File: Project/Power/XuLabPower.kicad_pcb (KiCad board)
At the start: 2 copper layers, 100 x 119 mm, 178 parts, among them J1 Servo, J10 Battery, J11 Battery, J12 Battery, J13 I2C, J14 SWD, J15 SPI1, J16 5V_2A, J17 5V_6A, J2 Servo, J3 Servo, J4 Servo, J5 Servo, J6 Servo, J7 Servo, J8 Servo, J9 Battery, Q1 SQJ138ELP, Q2 SQJ138ELP, Q3 SQJ138ELP, Q4 SQJ138ELP, Q5 SQJ138ELP, Q6 SQJ138ELP, SW1 SW_Push, U1 LM74502, U10 INA199B3DCKR, U11 TL331, U12 INA199B3DCKR, U13 TL331, U14 STM32L422KBTx, U15 TPS560200, U16 MIC5219-3.3YM5, U17 TPS562200, U18 TPS54627, U19 INA226, U2 NCV68061, U20 INA226, U21 INA226, U22 INA226, U23 INA226, U24 INA226, U25 INA226, U26 INA226, U3 NCV68061, U4 INA199B3DCKR, U5 TL331, U6 INA199B3DCKR, U7 TL331, U8 NCV68061, U9 NCV68061

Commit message: Add initial layout
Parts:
- C2: value 4700uF -> 2200uF; footprint Capacitor_THT:CP_Radial_D12.5mm_P5.00mm -> Capacitor_THT:CP_Radial_D18.0mm_P7.50mm
- J1, J2, J3, J4, J5, J6, J7, J8: footprint Connector_JST:JST_VH_S2P-VH_1x02_P3.96mm_Horizontal -> Connector_JST:JST_VH_B2P-VH_1x02_P3.96mm_Vertical
- J10, J11, J12, J9: footprint Connector_AMASS:AMASS_XT60PW-M_1x02_P7.20mm_Horizontal -> Connector_AMASS:AMASS_XT60-M_1x02_P7.20mm_Vertical
- moved H1 94.0 mm to (123.0, 105.0)
- moved H2 94.0 mm to (172.0, 105.0)
- moved H3 94.0 mm to (123.0, 47.0)
- moved H4 94.0 mm to (172.0, 47.0)
- moved C16 34.1 mm to (130.0, 48.0)
- moved SW1 34.1 mm to (135.0, 48.0)
- moved R39 33.0 mm to (143.0, 157.0), turned to 180 degrees
- moved R40 33.0 mm to (153.0, 123.0), turned to 0 degrees
- moved D1 31.3 mm to (120.0, 119.0), turned to 180 degrees
- moved D3 31.3 mm to (176.0, 161.0), turned to 0 degrees
- moved C10 30.5 mm to (164.0, 161.0), turned to 0 degrees
- moved C6 30.5 mm to (132.0, 119.0), turned to 180 degrees
- moved R12 30.0 mm to (124.0, 119.0), turned to 180 degrees
- moved R22 30.0 mm to (172.0, 161.0), turned to 0 degrees
- moved C13 28.0 mm to (152.0, 51.0)
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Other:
- board size 100 x 119 mm -> 74 x 148 mm

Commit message: Set stackup to six layers
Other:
- copper layers 2 -> 6
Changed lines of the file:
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@@
 	(layers
 		(0 "F.Cu" signal)
+		(4 "In1.Cu" power)
+		(6 "In2.Cu" power)
+		(8 "In3.Cu" power)
+		(10 "In4.Cu" power)
 		(2 "B.Cu" signal)
 		(9 "F.Adhes" user "F.Adhesive")
@@
 	)
 	(setup
+		(stackup
+			(layer "F.SilkS"
+				(type "Top Silk Screen")
+			)
+			(layer "F.Paste"
+				(type "Top Solder Paste")
+			)
+			(layer "F.Mask"
+				(type "Top Solder Mask")
+				(thickness 0.01)
+			)
+			(layer "F.Cu"
+				(type "copper")
+				(thickness 0.035)
+			)
+			(layer "dielectric 1"
+				(type "prepreg")
+				(thickness 0.1)
+				(material "FR4")
+				(epsilon_r 4.5)
+				(loss_tangent 0.02)
+			)
+			(layer "In1.Cu"
+				(type "copper")
+				(thickness 0.035)
+			)
+			(layer "dielectric 2"
+				(type "core")
+				(thickness 0.535)
+				(material "FR4")
+				(epsilon_r 4.5)
+				(loss_tangent 0.02)
+			)
+			(layer "In2.Cu"
+				(type "copper")
+				(thickness 0.035)
+			)
+			(layer "dielectric 3"
+				(type "prepreg")
+				(thickness 0.1)
+				(material "FR4")
+				(epsilon_r 4.5)
+				(loss_tangent 0.02)
+			)
+			(layer "In3.Cu"
+				(type "copper")
+				(thickness 0.035)
+			)
+			(layer "dielectric 4"
+				(type "core")
+				(thickness 0.535)
+				(material "FR4")
+				(epsilon_r 4.5)
+				(loss_tangent 0.02)
+			)
+			(layer "In4.Cu"
+				(type "copper")
+				(thickness 0.035)
+			)
+			(layer "dielectric 5"
+				(type "prepreg")
+				(thickness 0.1)
+				(material "FR4")
+				(epsilon_r 4.5)
+				(loss_tangent 0.02)
+			)
+			(layer "B.Cu"
+				(type "copper")
+				(thickness 0.035)
+			)
+			(layer "B.Mask"
+				(type "Bottom Solder Mask")
+				(thickness 0.01)
+			)
+			(layer "B.Paste"
+				(type "Bottom Solder Paste")
+			)
+			(layer "B.SilkS"
+				(type "Bottom Silk Screen")
+			)
+			(copper_finish "None")
+			(dielectric_constraints no)
+		)
 		(pad_to_mask_clearance 0)
 		(allow_soldermask_bridges_in_footprints no)

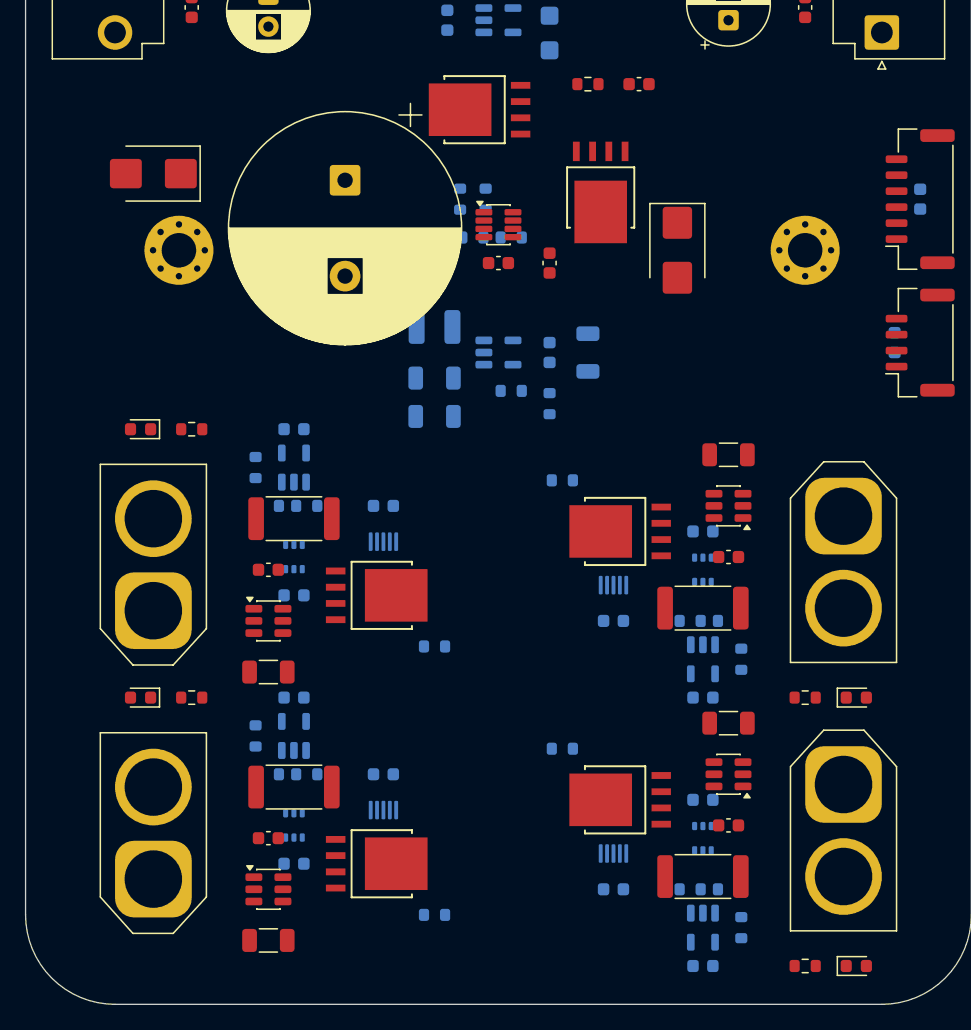
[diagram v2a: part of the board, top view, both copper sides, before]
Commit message: Add battery power routing
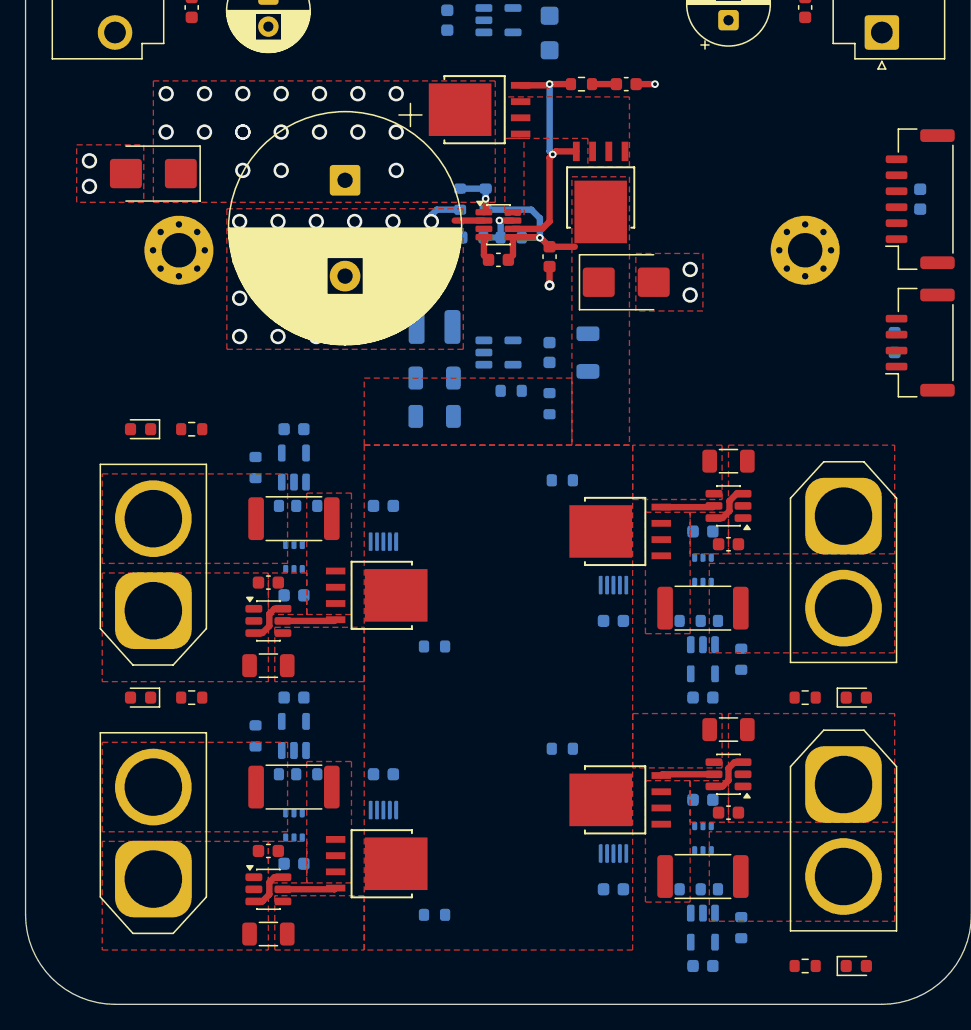
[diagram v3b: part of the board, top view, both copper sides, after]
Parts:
- moved D7 4.72 mm to (158.0, 107.5), turned to 0 degrees
- moved C3 1.00 mm to (158.0, 92.0)
- moved C63 1.00 mm to (130.0, 131.0)
- moved C65 1.00 mm to (130.0, 152.0)
- moved C67 1.00 mm to (166.0, 149.0)
- moved C69 1.00 mm to (166.0, 128.0)
- moved C1 0.50 mm to (152.0, 105.5)
- moved C64 0.50 mm to (130.0, 137.5)
- moved C66 0.50 mm to (130.0, 158.5)
- moved C68 0.50 mm to (166.0, 142.5)
- moved C70 0.50 mm to (166.0, 121.5)
- moved R1 0.50 mm to (154.5, 92.0)
- moved C4 0.25 mm to (148.0, 105.8)
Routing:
- net Net-(Q1-G): track 0.00 -> 20.0 mm, vias 0 -> 2
- net BATT_SRC: track 0.00 -> 14.6 mm, vias 0 -> 1
- net GND: track 0.00 -> 11.5 mm, vias 0 -> 25
- net Net-(Q6-G): track 0.00 -> 4.16 mm
- net Net-(Q5-G): track 0.00 -> 4.16 mm
- net Net-(Q4-G): track 0.00 -> 4.16 mm
- net Net-(Q3-G): track 0.00 -> 4.16 mm
- net /MAIN_EN: track 0.00 -> 3.91 mm, vias 0 -> 1
- net Net-(U1-OV): track 0.00 -> 3.78 mm, vias 0 -> 1
- net /SENS2-: track 0.00 -> 3.62 mm
- net /SENS1-: track 0.00 -> 3.62 mm
- net /SENS3-: track 0.00 -> 3.62 mm
- net /SENS4-: track 0.00 -> 3.52 mm
- net Net-(U1-VCAP): track 0.00 -> 1.93 mm
- net Net-(C3-Pad1): track 0.00 -> 1.90 mm
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- added copper zone on F.Cu, net +VSRC
- added copper zone on In2.Cu, net +VSRC
- added copper zone on F.Cu, net /SENS1+
- added copper zone on F.Cu, net /SENS1-
- added copper zone on F.Cu, net /SENS2+
- added copper zone on F.Cu, net /SENS2-
- added copper zone on F.Cu, net /SENS3+
- added copper zone on F.Cu, net /SENS3-
- added copper zone on F.Cu, net /SENS4+
- added copper zone on F.Cu, net /SENS4-
- added copper zone on F.Cu, net BATT_SRC
- added copper zone on F.Cu, net GND
- added copper zone on In1.Cu, net GND
- added copper zone on In4.Cu, net GND
- added copper zone on F.Cu, net Net-(U1-SRC)

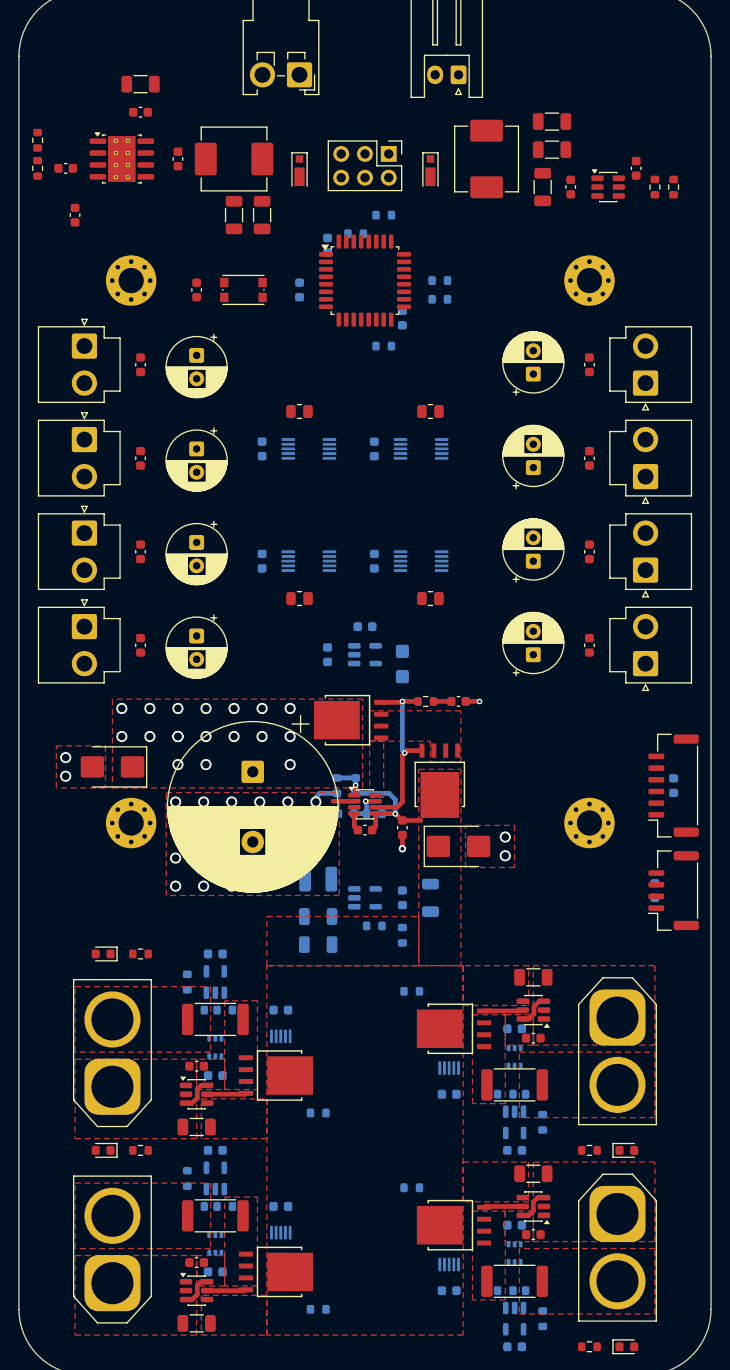
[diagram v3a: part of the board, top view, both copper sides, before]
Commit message: Add converter and motor power routing
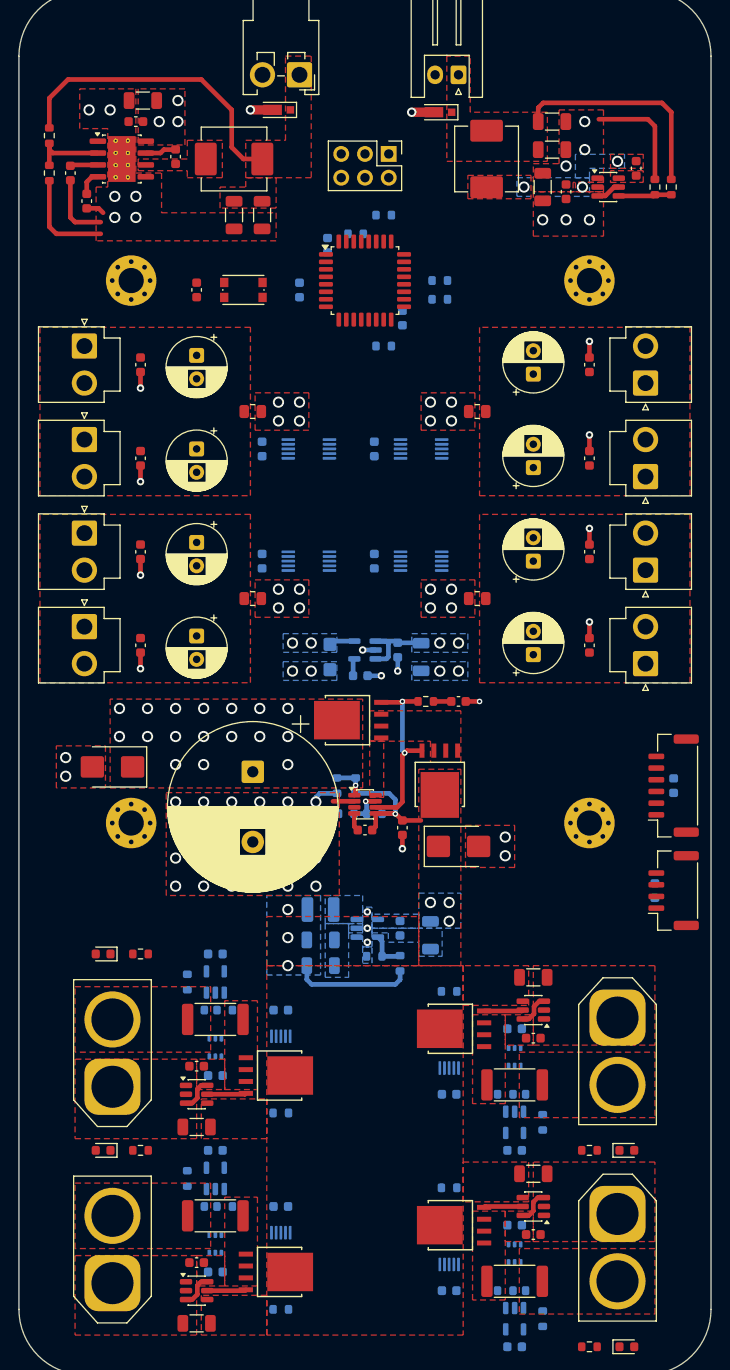
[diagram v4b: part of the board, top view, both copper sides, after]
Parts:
- added C31: 10uF, Capacitor_SMD:C_1206_3216Metric, B.Cu at (154.0, 87.2)
- moved C25 7.79 mm to (144.2, 87.2)
- moved C23 7.52 mm to (151.5, 86.5)
- moved D6 6.58 mm to (139.0, 28.8), turned to 180 degrees
- moved D5 6.15 mm to (156.2, 29.0), turned to 180 degrees
- moved C24 5.27 mm to (147.5, 89.2), turned to 0 degrees
- moved R41 5.00 mm to (136.0, 61.0)
- moved R42 5.00 mm to (136.0, 81.0)
- moved R43 5.00 mm to (160.0, 81.0)
- moved R44 5.00 mm to (160.0, 61.0)
- moved C19 4.00 mm to (155.0, 117.0)
- moved R37 4.00 mm to (139.0, 136.0)
- moved R38 4.00 mm to (157.0, 144.0)
- moved R39 4.00 mm to (139.0, 157.0)
- moved R40 4.00 mm to (157.0, 123.0)
- moved C20 3.26 mm to (151.8, 116.2)
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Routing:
- net GND: track 11.5 -> 66.8 mm, vias 25 -> 57
- net Net-(D6-K): track 0.00 -> 32.6 mm
- net Net-(D5-K): track 0.00 -> 23.5 mm
- net +5V: track 0.00 -> 22.2 mm, vias 0 -> 5
- net Net-(U18-VFB): track 0.00 -> 8.36 mm
- net Net-(U17-VFB): track 0.00 -> 5.66 mm
- net Net-(U15-FB): track 0.00 -> 4.19 mm
- net Net-(U18-VBST): track 0.00 -> 3.35 mm
- net Net-(U18-VREG): track 0.00 -> 2.97 mm
- net +3.3V: track 0.00 -> 2.97 mm, vias 0 -> 2
- net Net-(U18-SS): track 0.00 -> 2.68 mm
- net +VSRC: track 0.00 -> 2.67 mm, vias 18 -> 39
- net Net-(U16-BP): track 0.00 -> 1.86 mm
- net Net-(U17-SW): vias 0 -> 3
- net BATT_SRC: vias 1 -> 4
- added copper zone on B.Cu, net +3.3V
- added copper zone on B.Cu, net +5V
- added copper zone on F.Cu, net /SENS5-
- added copper zone on F.Cu, net /SENS6-
- added copper zone on F.Cu, net /SENS7-
- added copper zone on F.Cu, net /SENS8-
- added copper zone on B.Cu, net BATT_SRC
- added copper zone on B.Cu, net GND
- added copper zone on F.Cu, net Net-(D5-K)
- added copper zone on F.Cu, net Net-(D6-K)
- added copper zone on B.Cu, net Net-(U15-PH)
- added copper zone on B.Cu, net Net-(U17-SW)
- added copper zone on F.Cu, net Net-(U17-SW)
- added copper zone on F.Cu, net Net-(U17-VBST)
- added copper zone on F.Cu, net Net-(U18-SW)

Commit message: Add signal routing
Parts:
- moved C39 11.5 mm to (144.8, 135.0)
- moved C40 11.5 mm to (144.8, 156.0)
- moved C41 11.5 mm to (151.2, 145.0)
- moved C42 11.5 mm to (151.2, 124.0)
- moved C44 9.51 mm to (158.5, 65.5), turned to -90 degrees
- moved C46 9.51 mm to (158.5, 76.5), turned to -90 degrees
- moved R37 9.06 mm to (148.0, 135.0)
- moved R38 9.06 mm to (148.0, 145.0)
- moved R39 9.06 mm to (148.0, 156.0)
- moved R40 9.06 mm to (148.0, 124.0)
- moved U19 7.52 mm to (146.2, 132.0), turned to 180 degrees
- moved U20 7.52 mm to (146.2, 153.0), turned to 180 degrees
- moved U21 7.52 mm to (149.8, 148.0), turned to 0 degrees
- moved U22 7.52 mm to (149.8, 127.0), turned to 0 degrees
- moved C15 2.76 mm to (143.8, 48.2)
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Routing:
- net /Microcontroller/I2C3_SDA: track 0.00 -> 166.5 mm, vias 0 -> 16
- net /Microcontroller/I2C3_SCL: track 0.00 -> 143.0 mm, vias 0 -> 7
- net GND: track 66.8 -> 195.4 mm, vias 57 -> 89
- net /Microcontroller/GPIO_EXTI14: track 0.00 -> 118.4 mm, vias 0 -> 2
- net /Microcontroller/GPIO_EXTI2: track 0.00 -> 118.2 mm, vias 0 -> 2
- net /Microcontroller/GPIO_EXTI1: track 0.00 -> 100.3 mm, vias 0 -> 2
- net /Microcontroller/GPIO_EXTI15: track 0.00 -> 91.4 mm, vias 0 -> 2
- net /Microcontroller/I2C1_SCL: track 0.00 -> 86.8 mm, vias 0 -> 2
- net /Microcontroller/I2C1_SDA: track 0.00 -> 85.9 mm, vias 0 -> 2
- net /Microcontroller/SPI1_MOSI: track 0.00 -> 79.1 mm, vias 0 -> 2
- net /Microcontroller/SPI1_SCK: track 0.00 -> 78.5 mm, vias 0 -> 2
- net /Microcontroller/SPI1_MISO: track 0.00 -> 78.3 mm, vias 0 -> 2
- net /Microcontroller/SPI1_NSS: track 0.00 -> 76.3 mm, vias 0 -> 2
- net /MAIN_EN: track 3.91 -> 77.5 mm, vias 1 -> 2
- net +3.3V: track 2.97 -> 72.3 mm, vias 2 -> 28
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
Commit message: Add internal 5 and 3.3 V power layers
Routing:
- added copper zone on In5.Cu, net +3.3V
- added copper zone on In4.Cu, net +5V
- added copper zone on In6.Cu, net GND
- removed copper zone on In4.Cu, net GND
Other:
- copper layers 6 -> 8
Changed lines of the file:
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@@
 		(8 "In3.Cu" signal)
 		(10 "In4.Cu" power)
+		(12 "In5.Cu" power)
+		(14 "In6.Cu" power)
 		(2 "B.Cu" signal)
 		(9 "F.Adhes" user "F.Adhesive")
@@
 			(layer "dielectric 2"
 				(type "core")
-				(thickness 0.535)
+				(thickness 0.3)
 				(material "FR4")
 				(epsilon_r 4.5)
@@
 			(layer "dielectric 4"
 				(type "core")
-				(thickness 0.535)
+				(thickness 0.3)
 				(material "FR4")
 				(epsilon_r 4.5)
@@
 				(loss_tangent 0.02)
 			)
+			(layer "In5.Cu"
+				(type "copper")
+				(thickness 0.035)
+			)
+			(layer "dielectric 6"
+				(type "core")
+				(thickness 0.3)
+				(material "FR4")
+				(epsilon_r 4.5)
+				(loss_tangent 0.02)
+			)
+			(layer "In6.Cu"
+				(type "copper")
+				(thickness 0.035)
+			)
+			(layer "dielectric 7"
+				(type "prepreg")
+				(thickness 0.1)
+				(material "FR4")
+				(epsilon_r 4.5)
+				(loss_tangent 0.02)
+			)
 			(layer "B.Cu"
 				(type "copper")
@@
 	)
 	(zone
-		(net 2)
-		(net_name "GND")
+		(net 6)
+		(net_name "+5V")
 		(layer "In4.Cu")
 		(hatch edge 0.5)
@@
 		(connect_pads yes
 			(clearance 0.2)
+		)
+		(min_thickness 0.25)
+		(filled_areas_thickness no)
+		(fill yes
+			(thermal_gap 0.5)
+			(thermal_bridge_width 0.5)
+		)
+		(polygon
+			(pts
+				(xy 111 16) (xy 185 16) (xy 185 164) (xy 111 164)
+			)
+		)
+	)
+	(zone
+		(net 7)
+		(net_name "+3.3V")
+		(layer "In5.Cu")
+		(hatch edge 0.5)
+		(priority 64)
+		(connect_pads yes
+			(clearance 0.2)
+		)
+		(min_thickness 0.25)
+		(filled_areas_thickness no)
+		(fill yes
+			(thermal_gap 0.5)
+			(thermal_bridge_width 0.5)
+		)
+		(polygon
+			(pts
+				(xy 111 16) (xy 185 16) (xy 185 164) (xy 111 164)
+			)
+		)
+	)
+	(zone
+		(net 2)
+		(net_name "GND")
+		(layer "In6.Cu")
+		(hatch edge 0.5)
+		(priority 65)
+		(connect_pads yes
+			(clearance 0.2)
